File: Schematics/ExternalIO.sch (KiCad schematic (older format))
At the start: 49 parts, among them J4 AudioJack3_SwitchTR, J5 Conn_01x02, J6 Conn_01x08, SW2 Rotary_Encoder_Switch, SW3 Rotary_Encoder_Switch, SW4 Rotary_Encoder_Switch, SW5 Rotary_Encoder_Switch, SW6 SW_Push, SW7 SW_Push, SW8 SW_Push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

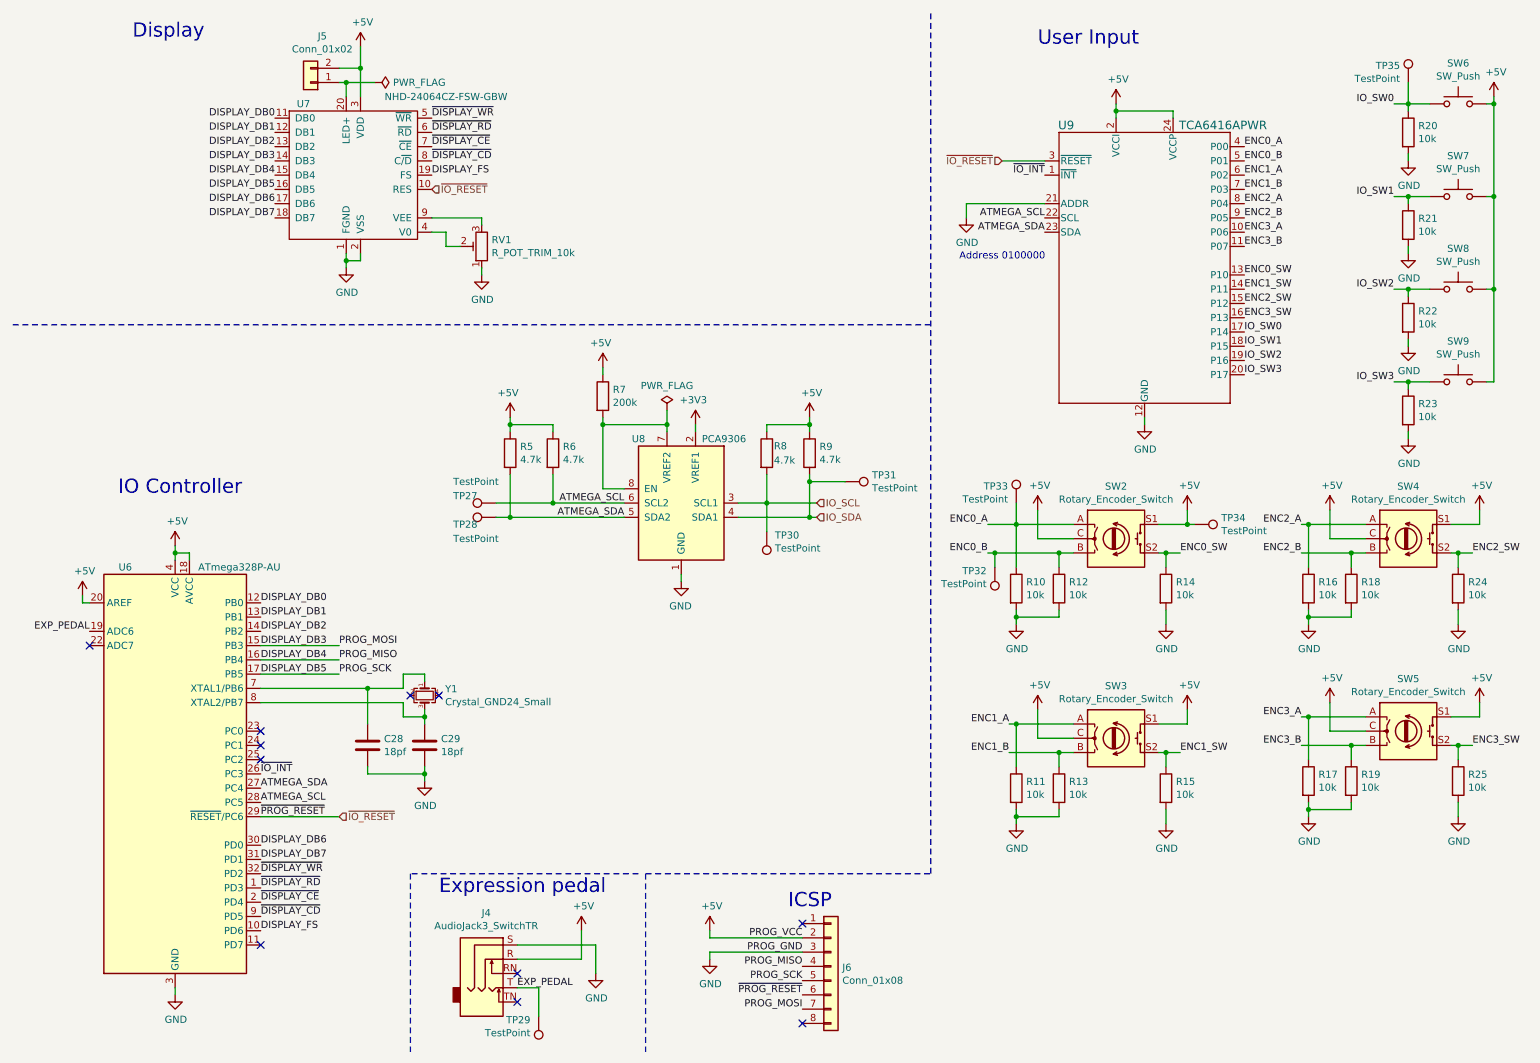
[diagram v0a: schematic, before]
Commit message: Finished initial component placement
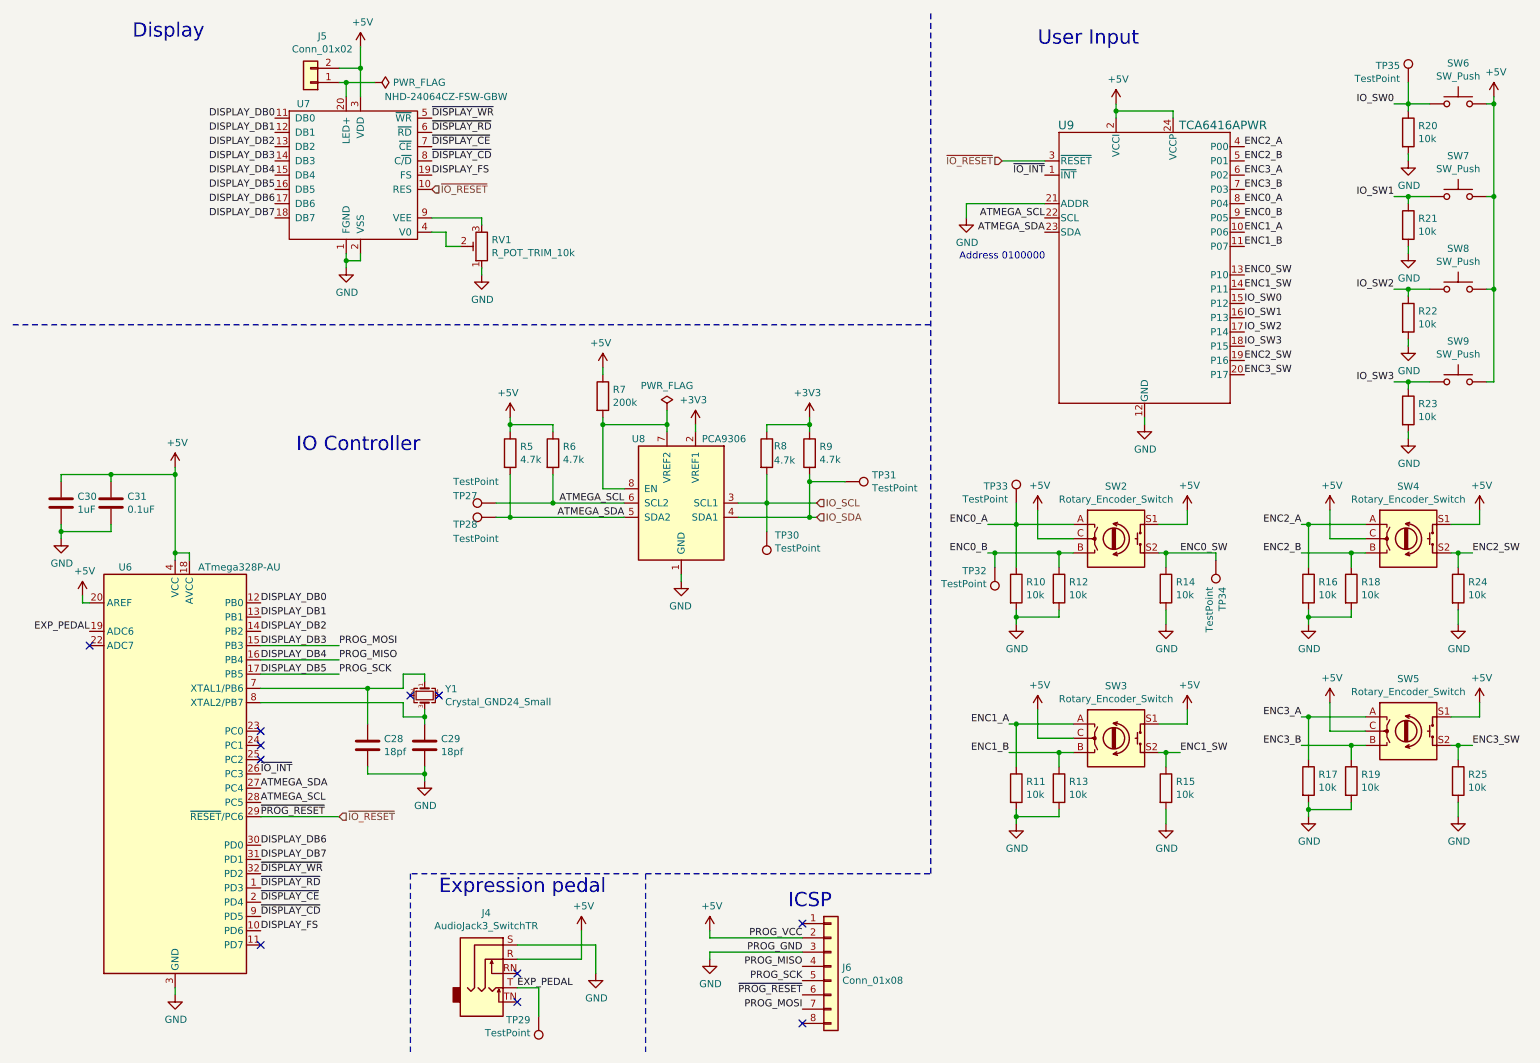
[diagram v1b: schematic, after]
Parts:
- added C30: 1uF, Capacitor_SMD:C_0805_2012Metric, symbol Device:C
- added C31: 0.1uF, Capacitor_SMD:C_0805_2012Metric, symbol Device:C
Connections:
- net +3V3: now also R8.1, R9.1
- net +5V: now also C30.2, C31.2; no longer R8.1, R9.1, TP34.1
- net ENC0_A: now also U9.8 (P04); no longer U9.4 (P00)
- net ENC0_B: now also U9.9 (P05); no longer U9.5 (P01)
- net ENC0_SW: now also TP34.1
- net ENC1_A: now also U9.10 (P06); no longer U9.6 (P02)
- net ENC1_B: now also U9.11 (P07); no longer U9.7 (P03)
- net ENC2_A: now also U9.4 (P00); no longer U9.8 (P04)
- net ENC2_B: now also U9.5 (P01); no longer U9.9 (P05)
- net ENC2_SW: now also U9.19 (P16); no longer U9.15 (P12)
- net ENC3_A: now also U9.6 (P02); no longer U9.10 (P06)
- net ENC3_B: now also U9.7 (P03); no longer U9.11 (P07)
- net ENC3_SW: now also U9.20 (P17); no longer U9.16 (P13)
- net GND: now also C30.1, C31.1
- net IO_SW0: now also U9.15 (P12); no longer U9.17 (P14)
- net IO_SW1: now also U9.16 (P13); no longer U9.18 (P15)
- net IO_SW2: now also U9.17 (P14); no longer U9.19 (P16)
- net IO_SW3: now also U9.18 (P15); no longer U9.20 (P17)
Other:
- moved on the sheet: TP34
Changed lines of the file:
@@
 Connection ~ 8600 4300
-Wire Wire Line
-	8600 4300 8700 4300
 Wire Wire Line
 	8550 4100 8750 4100
@@
 Text Label 10200 3100 2    50   ~ 0
 IO_SW3
+Text Label 9150 1850 0    50   ~ 0
+ENC0_A
+Text Label 9150 1950 0    50   ~ 0
+ENC0_B
+Text Label 9150 2050 0    50   ~ 0
+ENC1_A
+Text Label 9150 2150 0    50   ~ 0
+ENC1_B
 Text Label 9150 1450 0    50   ~ 0
-ENC0_A
+ENC2_A
 Text Label 9150 1550 0    50   ~ 0
-ENC0_B
+ENC2_B
 Text Label 9150 1650 0    50   ~ 0
-ENC1_A
+ENC3_A
 Text Label 9150 1750 0    50   ~ 0
-ENC1_B
-Text Label 9150 1850 0    50   ~ 0
-ENC2_A
-Text Label 9150 1950 0    50   ~ 0
-ENC2_B
-Text Label 9150 2050 0    50   ~ 0
-ENC3_A
-Text Label 9150 2150 0    50   ~ 0
 ENC3_B
 Text Label 9150 2350 0    50   ~ 0
@@
 Text Label 9150 2450 0    50   ~ 0
 ENC1_SW
+Text Label 9150 2950 0    50   ~ 0
+ENC2_SW
+Text Label 9150 3050 0    50   ~ 0
+ENC3_SW
 Text Label 9150 2550 0    50   ~ 0
-ENC2_SW
+IO_SW0
 Text Label 9150 2650 0    50   ~ 0
-ENC3_SW
+IO_SW1
 Text Label 9150 2750 0    50   ~ 0
-IO_SW0
+IO_SW2
 Text Label 9150 2850 0    50   ~ 0
-IO_SW1
-Text Label 9150 2950 0    50   ~ 0
-IO_SW2
-Text Label 9150 3050 0    50   ~ 0
 IO_SW3
 Wire Wire Line
@@
 L power:+5V #PWR039
 U 1 1 5EF544B0
-P 1650 4250
-F 0 "#PWR039" H 1650 4100 50  0001 C CNN
-F 1 "+5V" H 1665 4423 50  0000 C CNN
-F 2 "" H 1650 4250 50  0001 C CNN
-F 3 "" H 1650 4250 50  0001 C CNN
-	1    1650 4250
+P 1650 3700
+F 0 "#PWR039" H 1650 3550 50  0001 C CNN
+F 1 "+5V" H 1665 3873 50  0000 C CNN
+F 2 "" H 1650 3700 50  0001 C CNN
+F 3 "" H 1650 3700 50  0001 C CNN
+	1    1650 3700
 	1    0    0    -1
 $EndComp
@@
 Connection ~ 1650 4300
 Wire Wire Line
-	1650 4300 1650 4250
+	1650 4300 1650 3750
 Text HLabel 6150 4050 2    50   Input ~ 0
 IO_SDA
@@
 Wire Wire Line
 	5800 3950 5800 3750
-$Comp
-L power:+5V #PWR053
-U 1 1 5F0D62E3
-P 6100 3350
-F 0 "#PWR053" H 6100 3200 50  0001 C CNN
-F 1 "+5V" H 6115 3523 50  0000 C CNN
-F 2 "" H 6100 3350 50  0001 C CNN
-F 3 "" H 6100 3350 50  0001 C CNN
-	1    6100 3350
-	1    0    0    -1
-$EndComp
 Wire Wire Line
 	6100 3450 6100 3400
@@
 L Connector:TestPoint TP34
 U 1 1 5F66C142
-P 8800 4100
-F 0 "TP34" V 8846 4288 50  0000 L CNN
-F 1 "TestPoint" V 8755 4288 50  0000 L CNN
-F 2 "TestPoint:TestPoint_Keystone_5010-5014_Multipurpose" H 9000 4100 50  0001 C CNN
-F 3 "~" H 9000 4100 50  0001 C CNN
-	1    8800 4100
-	0    1    -1   0
-$EndComp
-Wire Wire Line
-	8800 4100 8750 4100
-Connection ~ 8750 4100
+P 8950 4350
+F 0 "TP34" V 8996 4538 50  0000 L CNN
+F 1 "TestPoint" V 8905 4538 50  0000 L CNN
+F 2 "TestPoint:TestPoint_Keystone_5010-5014_Multipurpose" H 9150 4350 50  0001 C CNN
+F 3 "~" H 9150 4350 50  0001 C CNN
+	1    8950 4350
+	1    0    0    1
+$EndComp
 $Comp
 L Connector:TestPoint TP33
@@
 Wire Wire Line
 	2950 900  2950 1100
-Text Notes 1250 3900 0    100  ~ 0
+Text Notes 2500 3600 0    100  ~ 0
 IO Controller
 $Comp
@@
 	3050 1000 2850 1000
 Connection ~ 2850 1000
+$Comp
+L power:+3V3 #PWR0102
+U 1 1 5F0927D7
+P 6100 3350
+F 0 "#PWR0102" H 6100 3200 50  0001 C CNN
+F 1 "+3V3" H 6115 3523 50  0000 C CNN
+F 2 "" H 6100 3350 50  0001 C CNN
+F 3 "" H 6100 3350 50  0001 C CNN
+	1    6100 3350
+	-1   0    0    -1
+$EndComp
+$Comp
+L Device:C C?
+U 1 1 5F12182E
+P 850 3950
+AR Path="/5EE67B04/5F12182E" Ref="C?"  Part="1"
+AR Path="/5EE77A0E/5F12182E" Ref="C30"  Part="1"
+F 0 "C30" H 735 3904 50  0000 R CNN
+F 1 "1uF" H 735 3995 50  0000 R CNN
+F 2 "Capacitor_SMD:C_0805_2012Metric" H 888 3800 50  0001 C CNN
+F 3 "~" H 850 3950 50  0001 C CNN
+F 4 "C28323" H 850 3950 50  0001 C CNN "LCSC Part #"
+	1    850  3950
+	-1   0    0    1
+$EndComp
+$Comp
+L Device:C C?
+U 1 1 5F121835
+P 1200 3950
+AR Path="/5EE67B04/5F121835" Ref="C?"  Part="1"
+AR Path="/5EE77A0E/5F121835" Ref="C31"  Part="1"
+F 0 "C31" H 1085 3904 50  0000 R CNN
+F 1 "0.1uF" H 1085 3995 50  0000 R CNN
+F 2 "Capacitor_SMD:C_0805_2012Metric" H 1238 3800 50  0001 C CNN
+F 3 "~" H 1200 3950 50  0001 C CNN
+F 4 "C28233" H 1200 3950 50  0001 C CNN "LCSC Part #"
+	1    1200 3950
+	-1   0    0    1
+$EndComp
+$Comp
+L power:GND #PWR053
+U 1 1 5F1484CF
+P 850 4200
+F 0 "#PWR053" H 850 3950 50  0001 C CNN
+F 1 "GND" H 855 4027 50  0000 C CNN
+F 2 "" H 850 4200 50  0001 C CNN
+F 3 "" H 850 4200 50  0001 C CNN
+	1    850  4200
+	1    0    0    -1
+$EndComp
+Wire Wire Line
+	1650 3750 1200 3750
+Wire Wire Line
+	850  3750 850  3800
+Connection ~ 1650 3750
+Wire Wire Line
+	1650 3750 1650 3700
+Wire Wire Line
+	1200 3800 1200 3750
+Connection ~ 1200 3750
+Wire Wire Line
+	1200 3750 850  3750
+Wire Wire Line
+	850  4100 850  4150
+Wire Wire Line
+	850  4150 1200 4150
+Wire Wire Line
+	1200 4150 1200 4100
+Connection ~ 850  4150
+Wire Wire Line
+	850  4150 850  4200
+Wire Wire Line
+	8950 4300 8950 4350
+Wire Wire Line
+	8600 4300 8950 4300
 $EndSCHEMATC
